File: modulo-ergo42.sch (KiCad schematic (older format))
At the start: 4 parts

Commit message: Design schematic
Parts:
- added J3: AudioJack4_Ground, library:TRRS_SMD_PJ320, symbol Connector:AudioJack4_Ground
- added R1, R2, R3: 10 kΩ, Resistor_SMD:R_0603_1608Metric, symbol Device:R
- added SW1, SW10, SW11, SW12, SW13, SW14, SW15, SW16, SW17, SW18, SW19, SW2, SW20, SW21, SW22, SW23, SW24, SW25, SW26, SW27, SW28, SW3, SW4, SW5, SW6, SW7, SW8, SW9: SW_Push, library:Kailh_Socket, symbol Switch:SW_Push
- added SW29: SW_DIP_x02, library:DipSwitch, symbol Switch:SW_DIP_x02
- J1, J2: renamed from J?; footprint (none) -> library:TRRS_SMD_PJ320
- gave numbers to parts that had none: 2
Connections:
- net 3V3: now also J3.T
- net GND: now also U1.21 (A0), J3.S, SW1.1, SW10.1, SW11.1, SW12.1, SW13.1, SW14.1, SW15.1, SW16.1, SW17.1, SW18.1, SW19.1, SW2.1, SW20.1, SW21.1, SW22.1, SW23.1, SW24.1, SW25.1, SW26.1, SW27.1, SW28.1, SW29.3, SW29.4, SW3.1, SW4.1, SW5.1, SW6.1, SW7.1, SW8.1, SW9.1
- net SCL1: now also U1.22 (SCL)
- net SCL2: now also U2.22 (SCL)
- net SDA1: now also U1.23 (SDA)
- net SDA2: now also U2.23 (SDA)
- net VCC: now also U2.21 (A0), R1.1, R2.1, R3.1
- net INT: now reaches U1.1 (~INT)
- net INT: now also U2.1 (~INT), J3.R1, R1.2
- net R3C2: now reaches U1.10 (P06)
- net R3C2: now also SW7.2
- net R4C2: now reaches U1.11 (P07)
- net R4C2: now also SW8.2
- net R1C3: now reaches U1.13 (P10)
- net R1C3: now also SW9.2
- net R2C3: now reaches U1.14 (P11)
- net R2C3: now also SW10.2
- net R3C3: now reaches U1.15 (P12)
- net R3C3: now also SW11.2
- net R4C3: now reaches U1.16 (P13)
- net R4C3: now also SW12.2
- net R1C4: now reaches U1.17 (P14)
- net R1C4: now also SW13.2
- net R2C4: now reaches U1.18 (P15)
- net R2C4: now also SW14.2
- net R3C4: now reaches U1.19 (P16)
- net R3C4: now also SW15.2
- net A1: now reaches U1.2 (A1)
- net A1: now also U2.2 (A1), R2.2, SW29.2
- net R4C4: now reaches U1.20 (P17)
- net R4C4: now also SW16.2
- net A2: now reaches U1.3 (A2)
- net A2: now also U2.3 (A2), R3.2, SW29.1
- net R1C1: now reaches U1.4 (P00)
- net R1C1: now also SW1.2
- net R2C1: now reaches U1.5 (P01)
- net R2C1: now also SW2.2
- net R3C1: now reaches U1.6 (P02)
- net R3C1: now also SW3.2
- net R4C1: now reaches U1.7 (P03)
- net R4C1: now also SW4.2
- net R1C2: now reaches U1.8 (P04)
- net R1C2: now also SW5.2
- net R2C2: now reaches U1.9 (P05)
- net R2C2: now also SW6.2
- net R3C6: now reaches U2.10 (P06)
- net R3C6: now also SW23.2
- net R4C6: now reaches U2.11 (P07)
- net R4C6: now also SW24.2
- net R1C7: now reaches U2.13 (P10)
- net R1C7: now also SW25.2
- net R2C7: now reaches U2.14 (P11)
- net R2C7: now also SW26.2
- net R3C7: now reaches U2.15 (P12)
- net R3C7: now also SW27.2
- net R4C7: now reaches U2.16 (P13)
- net R4C7: now also SW28.2
- net R1C5: now reaches U2.4 (P00)
- net R1C5: now also SW17.2
- net R2C5: now reaches U2.5 (P01)
- net R2C5: now also SW18.2
- net R3C5: now reaches U2.6 (P02)
- net R3C5: now also SW19.2
- net R4C5: now reaches U2.7 (P03)
- net R4C5: now also SW20.2
- net R1C6: now reaches U2.8 (P04)
- net R1C6: now also SW21.2
- net R2C6: now reaches U2.9 (P05)
- net R2C6: now also SW22.2
- no-connect marks 0 -> 5
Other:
- moved on the sheet: J1, J2, U1, U2

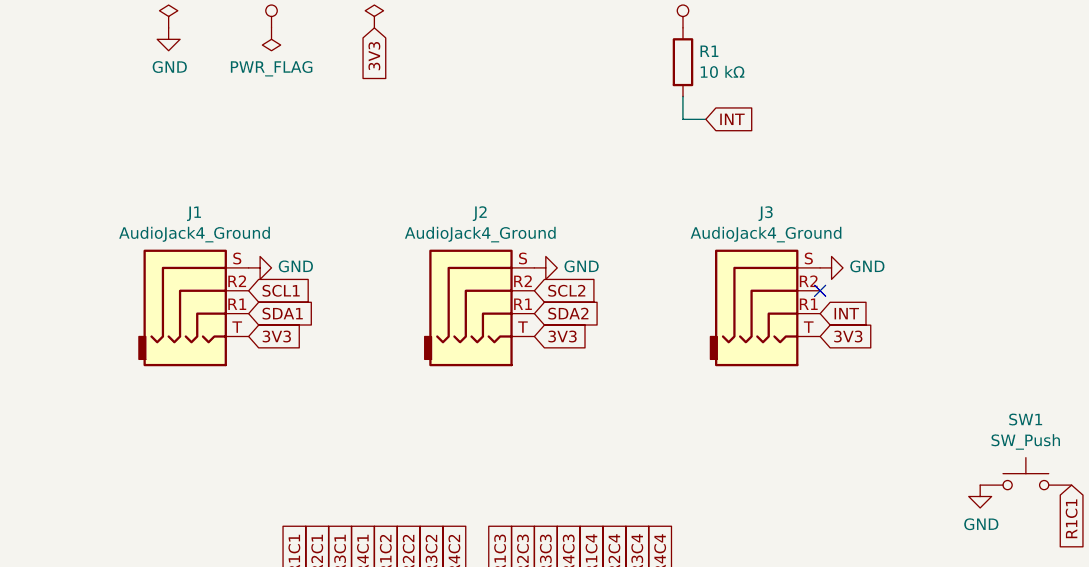
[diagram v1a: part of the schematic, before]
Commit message: Add int socket
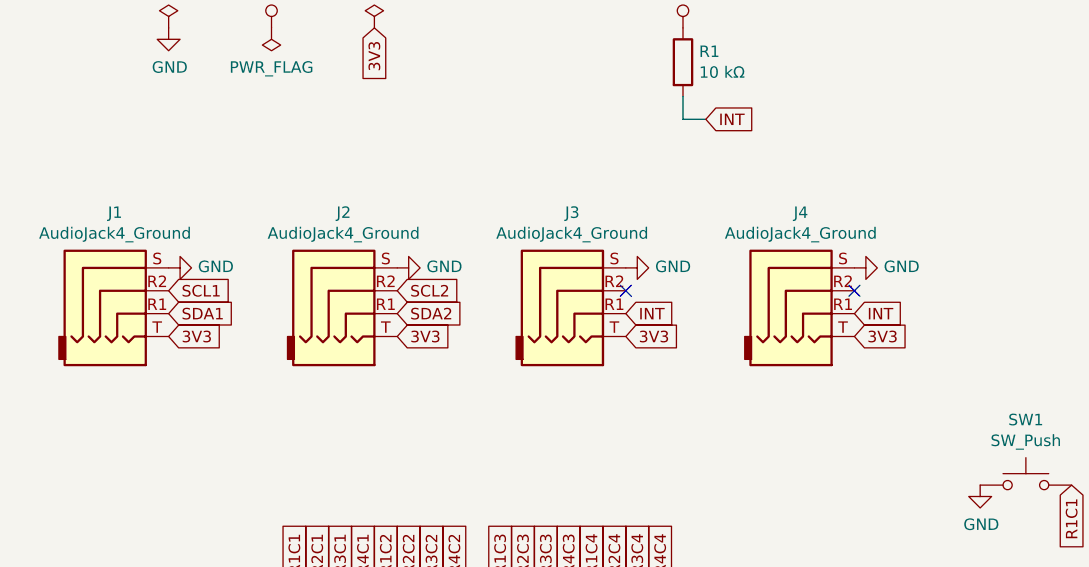
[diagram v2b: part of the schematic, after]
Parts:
- added J4: AudioJack4_Ground, library:TRRS_SMD_PJ320, symbol Connector:AudioJack4_Ground
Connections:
- net 3V3: now also J4.T
- net GND: now also J4.S
- net INT: now also J4.R1
- no-connect marks 5 -> 6
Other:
- moved on the sheet: J1, J2, J3
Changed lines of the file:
@@
 L Connector:AudioJack4_Ground J1
 U 1 1 5BC2FF07
-P 1350 2200
-F 0 "J1" H 1316 2542 50  0000 C CNN
-F 1 "AudioJack4_Ground" H 1316 2451 50  0000 C CNN
-F 2 "library:TRRS_SMD_PJ320" H 1350 2200 50  0001 C CNN
-F 3 "~" H 1350 2200 50  0001 C CNN
-	1    1350 2200
+P 1000 2200
+F 0 "J1" H 966 2542 50  0000 C CNN
+F 1 "AudioJack4_Ground" H 966 2451 50  0000 C CNN
+F 2 "library:TRRS_SMD_PJ320" H 1000 2200 50  0001 C CNN
+F 3 "~" H 1000 2200 50  0001 C CNN
+	1    1000 2200
 	1    0    0    -1
 $EndComp
@@
 L Connector:AudioJack4_Ground J2
 U 1 1 5BC30075
-P 2600 2200
-F 0 "J2" H 2566 2542 50  0000 C CNN
-F 1 "AudioJack4_Ground" H 2566 2451 50  0000 C CNN
-F 2 "library:TRRS_SMD_PJ320" H 2600 2200 50  0001 C CNN
-F 3 "~" H 2600 2200 50  0001 C CNN
-	1    2600 2200
+P 2000 2200
+F 0 "J2" H 1966 2542 50  0000 C CNN
+F 1 "AudioJack4_Ground" H 1966 2451 50  0000 C CNN
+F 2 "library:TRRS_SMD_PJ320" H 2000 2200 50  0001 C CNN
+F 3 "~" H 2000 2200 50  0001 C CNN
+	1    2000 2200
 	1    0    0    -1
 $EndComp
@@
 	0    -1   -1   0
 $EndComp
-Text GLabel 1550 2400 2    50   Input ~ 0
+Text GLabel 1200 2400 2    50   Input ~ 0
 3V3
-Text GLabel 2800 2400 2    50   Input ~ 0
+Text GLabel 2200 2400 2    50   Input ~ 0
 3V3
 $Comp
 L power:GND #PWR02
 U 1 1 5BC31239
-P 1550 2100
-F 0 "#PWR02" H 1550 1850 50  0001 C CNN
-F 1 "GND" V 1555 1972 50  0000 R CNN
-F 2 "" H 1550 2100 50  0001 C CNN
-F 3 "" H 1550 2100 50  0001 C CNN
-	1    1550 2100
+P 1200 2100
+F 0 "#PWR02" H 1200 1850 50  0001 C CNN
+F 1 "GND" V 1205 1972 50  0000 R CNN
+F 2 "" H 1200 2100 50  0001 C CNN
+F 3 "" H 1200 2100 50  0001 C CNN
+	1    1200 2100
 	0    -1   -1   0
 $EndComp
@@
 L power:GND #PWR05
 U 1 1 5BC31273
-P 2800 2100
-F 0 "#PWR05" H 2800 1850 50  0001 C CNN
-F 1 "GND" V 2805 1972 50  0000 R CNN
-F 2 "" H 2800 2100 50  0001 C CNN
-F 3 "" H 2800 2100 50  0001 C CNN
-	1    2800 2100
+P 2200 2100
+F 0 "#PWR05" H 2200 1850 50  0001 C CNN
+F 1 "GND" V 2205 1972 50  0000 R CNN
+F 2 "" H 2200 2100 50  0001 C CNN
+F 3 "" H 2200 2100 50  0001 C CNN
+	1    2200 2100
 	0    -1   -1   0
 $EndComp
-Text GLabel 1550 2200 2    50   Input ~ 0
+Text GLabel 1200 2200 2    50   Input ~ 0
 SCL1
-Text GLabel 1550 2300 2    50   Input ~ 0
+Text GLabel 1200 2300 2    50   Input ~ 0
 SDA1
-Text GLabel 2800 2200 2    50   Input ~ 0
+Text GLabel 2200 2200 2    50   Input ~ 0
 SCL2
-Text GLabel 2800 2300 2    50   Input ~ 0
+Text GLabel 2200 2300 2    50   Input ~ 0
 SDA2
 $Comp
@@
 L Connector:AudioJack4_Ground J3
 U 1 1 5BC32F04
-P 3850 2200
-F 0 "J3" H 3816 2542 50  0000 C CNN
-F 1 "AudioJack4_Ground" H 3816 2451 50  0000 C CNN
-F 2 "library:TRRS_SMD_PJ320" H 3850 2200 50  0001 C CNN
-F 3 "~" H 3850 2200 50  0001 C CNN
-	1    3850 2200
+P 3000 2200
+F 0 "J3" H 2966 2542 50  0000 C CNN
+F 1 "AudioJack4_Ground" H 2966 2451 50  0000 C CNN
+F 2 "library:TRRS_SMD_PJ320" H 3000 2200 50  0001 C CNN
+F 3 "~" H 3000 2200 50  0001 C CNN
+	1    3000 2200
 	1    0    0    -1
 $EndComp
@@
 L power:GND #PWR010
 U 1 1 5BC33189
-P 4050 2100
-F 0 "#PWR010" H 4050 1850 50  0001 C CNN
-F 1 "GND" V 4055 1972 50  0000 R CNN
-F 2 "" H 4050 2100 50  0001 C CNN
-F 3 "" H 4050 2100 50  0001 C CNN
-	1    4050 2100
+P 3200 2100
+F 0 "#PWR010" H 3200 1850 50  0001 C CNN
+F 1 "GND" V 3205 1972 50  0000 R CNN
+F 2 "" H 3200 2100 50  0001 C CNN
+F 3 "" H 3200 2100 50  0001 C CNN
+	1    3200 2100
 	0    -1   -1   0
 $EndComp
-Text GLabel 4050 2400 2    50   Input ~ 0
+Text GLabel 3200 2400 2    50   Input ~ 0
 3V3
-Text GLabel 4050 2300 2    50   Input ~ 0
+Text GLabel 3200 2300 2    50   Input ~ 0
 INT
-NoConn ~ 4050 2200
+NoConn ~ 3200 2200
 Text GLabel 1950 4900 3    50   Input ~ 0
 INT
@@
 Text GLabel 2100 1050 3    50   Input ~ 0
 3V3
+$Comp
+L Connector:AudioJack4_Ground J4
+U 1 1 5BC43221
+P 4000 2200
+F 0 "J4" H 3966 2542 50  0000 C CNN
+F 1 "AudioJack4_Ground" H 3966 2451 50  0000 C CNN
+F 2 "library:TRRS_SMD_PJ320" H 4000 2200 50  0001 C CNN
+F 3 "~" H 4000 2200 50  0001 C CNN
+	1    4000 2200
+	1    0    0    -1
+$EndComp
+$Comp
+L power:GND #PWR042
+U 1 1 5BC4348C
+P 4200 2100
+F 0 "#PWR042" H 4200 1850 50  0001 C CNN
+F 1 "GND" V 4205 1972 50  0000 R CNN
+F 2 "" H 4200 2100 50  0001 C CNN
+F 3 "" H 4200 2100 50  0001 C CNN
+	1    4200 2100
+	0    -1   -1   0
+$EndComp
+NoConn ~ 4200 2200
+Text GLabel 4200 2300 2    50   Input ~ 0
+INT
+Text GLabel 4200 2400 2    50   Input ~ 0
+3V3
 $EndSCHEMATC

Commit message: Re-place parts for drill
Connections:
- net R1C1: now also U1.7 (P03); no longer U1.4 (P00)
- net R1C2: now also U1.11 (P07); no longer U1.8 (P04)
- net R1C5: now also U2.7 (P03); no longer U2.4 (P00)
- net R1C6: now also U2.11 (P07); no longer U2.8 (P04)
- net R2C1: now also U1.6 (P02); no longer U1.5 (P01)
- net R2C2: now also U1.10 (P06); no longer U1.9 (P05)
- net R2C5: now also U2.6 (P02); no longer U2.5 (P01)
- net R2C6: now also U2.10 (P06); no longer U2.9 (P05)
- net R3C1: now also U1.5 (P01); no longer U1.6 (P02)
- net R3C2: now also U1.9 (P05); no longer U1.10 (P06)
- net R3C5: now also U2.5 (P01); no longer U2.6 (P02)
- net R3C6: now also U2.9 (P05); no longer U2.10 (P06)
- net R4C1: now also U1.4 (P00); no longer U1.7 (P03)
- net R4C2: now also U1.8 (P04); no longer U1.11 (P07)
- net R4C5: now also U2.4 (P00); no longer U2.7 (P03)
- net R4C6: now also U2.8 (P04); no longer U2.11 (P07)
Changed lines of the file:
@@
 EESchema Schematic File Version 4
+LIBS:modulo-ergo42-cache
 EELAYER 26 0
 EELAYER END
@@
 NoConn ~ 3350 5800
 NoConn ~ 3150 5800
+Text GLabel 2050 3500 1    50   Input ~ 0
+R1C1
+Text GLabel 2450 3500 1    50   Input ~ 0
+R1C2
+Text GLabel 1950 3500 1    50   Input ~ 0
+R2C1
+Text GLabel 1850 3500 1    50   Input ~ 0
+R3C1
 Text GLabel 1750 3500 1    50   Input ~ 0
-R1C1
+R4C1
+Text GLabel 2350 3500 1    50   Input ~ 0
+R2C2
+Text GLabel 2250 3500 1    50   Input ~ 0
+R3C2
 Text GLabel 2150 3500 1    50   Input ~ 0
-R1C2
-Text GLabel 1850 3500 1    50   Input ~ 0
-R2C1
-Text GLabel 1950 3500 1    50   Input ~ 0
-R3C1
-Text GLabel 2050 3500 1    50   Input ~ 0
-R4C1
-Text GLabel 2250 3500 1    50   Input ~ 0
-R2C2
-Text GLabel 2350 3500 1    50   Input ~ 0
-R3C2
-Text GLabel 2450 3500 1    50   Input ~ 0
 R4C2
 Text GLabel 2650 3500 1    50   Input ~ 0
@@
 Text GLabel 3350 3500 1    50   Input ~ 0
 R4C4
+Text GLabel 2050 5800 1    50   Input ~ 0
+R1C5
+Text GLabel 1950 5800 1    50   Input ~ 0
+R2C5
+Text GLabel 1850 5800 1    50   Input ~ 0
+R3C5
 Text GLabel 1750 5800 1    50   Input ~ 0
-R1C5
-Text GLabel 1850 5800 1    50   Input ~ 0
-R2C5
-Text GLabel 1950 5800 1    50   Input ~ 0
-R3C5
-Text GLabel 2050 5800 1    50   Input ~ 0
 R4C5
+Text GLabel 2450 5800 1    50   Input ~ 0
+R1C6
+Text GLabel 2350 5800 1    50   Input ~ 0
+R2C6
+Text GLabel 2250 5800 1    50   Input ~ 0
+R3C6
 Text GLabel 2150 5800 1    50   Input ~ 0
-R1C6
-Text GLabel 2250 5800 1    50   Input ~ 0
-R2C6
-Text GLabel 2350 5800 1    50   Input ~ 0
-R3C6
-Text GLabel 2450 5800 1    50   Input ~ 0
 R4C6
 Text GLabel 2650 5800 1    50   Input ~ 0

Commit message: Fix schematics
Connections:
- net 3V3 is gone; now on net VCC: J1.T, J2.T, J3.T, J4.T, U1.24 (VCC), U2.24 (VCC)
- net SCL2 is gone; now on net SCL: J2.R2, U2.22 (SCL)
- net SDA2 is gone; now on net SDA: J2.R1, U2.23 (SDA)
- net SCL1 renamed SCL
- net SDA1 renamed SDA
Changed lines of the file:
@@
 $EndComp
 Text GLabel 1200 2200 2    50   Input ~ 0
-SCL1
+SCL
 Text GLabel 1200 2300 2    50   Input ~ 0
-SDA1
+SDA
 Text GLabel 2200 2200 2    50   Input ~ 0
-SCL2
+SCL
 Text GLabel 2200 2300 2    50   Input ~ 0
-SDA2
+SDA
 $Comp
 L power:GND #PWR08
@@
 	3450 1450 3550 1450
 Text GLabel 1850 4900 3    50   Input ~ 0
-SCL1
+SCL
 Text GLabel 1750 4900 3    50   Input ~ 0
-SDA1
+SDA
 Text GLabel 1850 7200 3    50   Input ~ 0
-SCL2
+SCL
 Text GLabel 1750 7200 3    50   Input ~ 0
-SDA2
+SDA
 $Comp
 L power:GND #PWR06
@@
 Text GLabel 9350 5400 3    50   Input ~ 0
 R4C7
-$Comp
-L power:PWR_FLAG #FLG03
-U 1 1 5BC41E23
-P 2100 1050
-F 0 "#FLG03" H 2100 1125 50  0001 C CNN
-F 1 "PWR_FLAG" H 2100 1224 50  0000 C CNN
-F 2 "" H 2100 1050 50  0001 C CNN
-F 3 "~" H 2100 1050 50  0001 C CNN
-	1    2100 1050
-	1    0    0    -1
-$EndComp
 Text GLabel 2100 1050 3    50   Input ~ 0
 3V3
@@
 Text GLabel 4200 2400 2    50   Input ~ 0
 3V3
+$Comp
+L power:VCC #PWR0101
+U 1 1 5BCCB118
+P 2100 1050
+F 0 "#PWR0101" H 2100 900 50  0001 C CNN
+F 1 "VCC" H 2117 1223 50  0000 C CNN
+F 2 "" H 2100 1050 50  0001 C CNN
+F 3 "" H 2100 1050 50  0001 C CNN
+	1    2100 1050
+	1    0    0    -1
+$EndComp
 $EndSCHEMATC
